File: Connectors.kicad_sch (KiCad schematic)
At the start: 4 parts

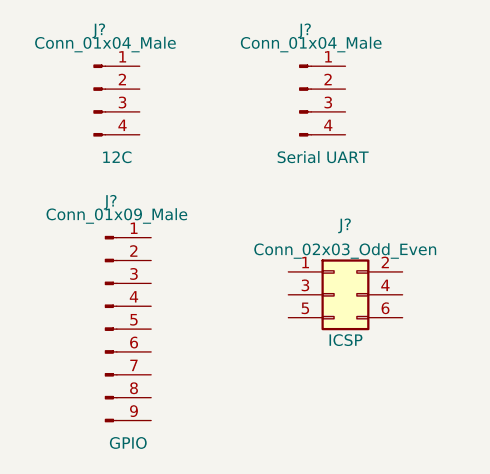
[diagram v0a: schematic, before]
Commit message: Changed locations of symbols
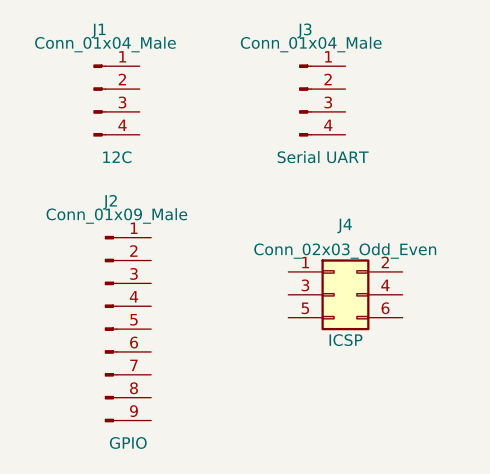
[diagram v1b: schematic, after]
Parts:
- gave numbers to parts that had none: 4
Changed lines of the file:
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@@
   (symbol (lib_id "Connector_Generic:Conn_02x03_Odd_Even") (at 111.76 92.71 0) (unit 1)
     (in_bom yes) (on_board yes)
-    (property "Reference" "J?" (id 0) (at 113.03 84.9335 0))
+    (property "Reference" "J4" (id 0) (at 113.03 84.9335 0))
     (property "Value" "Conn_02x03_Odd_Even" (id 1) (at 113.03 87.7086 0))
     (property "Footprint" "" (id 2) (at 111.76 92.71 0)
@@
   (symbol (lib_id "Connector:Conn_01x04_Male") (at 107.95 69.85 0) (unit 1)
     (in_bom yes) (on_board yes)
-    (property "Reference" "J?" (id 0) (at 108.585 63.2673 0))
+    (property "Reference" "J3" (id 0) (at 108.585 63.2673 0))
     (property "Value" "Conn_01x04_Male" (id 1) (at 109.22 64.77 0))
     (property "Footprint" "" (id 2) (at 107.95 69.85 0)
@@
   (symbol (lib_id "Connector:Conn_01x09_Male") (at 86.36 96.52 0) (unit 1)
     (in_bom yes) (on_board yes)
-    (property "Reference" "J?" (id 0) (at 86.995 82.3173 0))
+    (property "Reference" "J2" (id 0) (at 86.995 82.3173 0))
     (property "Value" "Conn_01x09_Male" (id 1) (at 87.63 83.82 0))
     (property "Footprint" "" (id 2) (at 86.36 96.52 0)
@@
   (symbol (lib_id "Connector:Conn_01x04_Male") (at 85.09 69.85 0) (unit 1)
     (in_bom yes) (on_board yes)
-    (property "Reference" "J?" (id 0) (at 85.725 63.2673 0))
+    (property "Reference" "J1" (id 0) (at 85.725 63.2673 0))
     (property "Value" "Conn_01x04_Male" (id 1) (at 86.36 64.77 0))
     (property "Footprint" "" (id 2) (at 85.09 69.85 0)

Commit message: Completed symbol-footprint associations
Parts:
- J1, J3: footprint (none) -> Connector_PinHeader_2.54mm:PinHeader_1x04_P2.54mm_Vertical
- J2: footprint (none) -> Connector_PinHeader_2.54mm:PinHeader_1x09_P2.54mm_Vertical
- J4: footprint (none) -> Connector_PinHeader_2.54mm:PinHeader_2x03_P2.54mm_Vertical
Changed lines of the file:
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@@
     (property "Reference" "J4" (id 0) (at 113.03 84.9335 0))
     (property "Value" "Conn_02x03_Odd_Even" (id 1) (at 113.03 87.7086 0))
-    (property "Footprint" "" (id 2) (at 111.76 92.71 0)
+    (property "Footprint" "Connector_PinHeader_2.54mm:PinHeader_2x03_P2.54mm_Vertical" (id 2) (at 111.76 92.71 0)
       (effects (font (size 1.27 1.27)) hide)
     )
@@
     (property "Reference" "J3" (id 0) (at 108.585 63.2673 0))
     (property "Value" "Conn_01x04_Male" (id 1) (at 109.22 64.77 0))
-    (property "Footprint" "" (id 2) (at 107.95 69.85 0)
+    (property "Footprint" "Connector_PinHeader_2.54mm:PinHeader_1x04_P2.54mm_Vertical" (id 2) (at 107.95 69.85 0)
       (effects (font (size 1.27 1.27)) hide)
     )
@@
     (property "Reference" "J2" (id 0) (at 86.995 82.3173 0))
     (property "Value" "Conn_01x09_Male" (id 1) (at 87.63 83.82 0))
-    (property "Footprint" "" (id 2) (at 86.36 96.52 0)
+    (property "Footprint" "Connector_PinHeader_2.54mm:PinHeader_1x09_P2.54mm_Vertical" (id 2) (at 86.36 96.52 0)
       (effects (font (size 1.27 1.27)) hide)
     )
@@
     (property "Reference" "J1" (id 0) (at 85.725 63.2673 0))
     (property "Value" "Conn_01x04_Male" (id 1) (at 86.36 64.77 0))
-    (property "Footprint" "" (id 2) (at 85.09 69.85 0)
+    (property "Footprint" "Connector_PinHeader_2.54mm:PinHeader_1x04_P2.54mm_Vertical" (id 2) (at 85.09 69.85 0)
       (effects (font (size 1.27 1.27)) hide)
     )

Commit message: final Wiring
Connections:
- net MISO: now reaches J4.1 (Pin_1)
- net Vcc: now reaches J4.2 (Pin_2)
- net Vcc: now also J1.2 (Pin_2), J2.9 (Pin_9), J3.2 (Pin_2)
- net SCK: now reaches J4.3 (Pin_3)
- net SCK: now also J1.4 (Pin_4)
- net MOSI: now reaches J4.4 (Pin_4)
- net RESET: now reaches J4.5 (Pin_5)
- net GND: now reaches J4.6 (Pin_6)
- net GND: now also J1.1 (Pin_1), J2.8 (Pin_8), J3.1 (Pin_1)
- net RX: now reaches J3.3 (Pin_3)
- net TX: now reaches J3.4 (Pin_4)
- net D2: now reaches J2.1 (Pin_1)
- net D3: now reaches J2.2 (Pin_2)
- net D4: now reaches J2.3 (Pin_3)
- net D5: now reaches J2.4 (Pin_4)
- net D6: now reaches J2.5 (Pin_5)
- net D7: now reaches J2.6 (Pin_6)
- net D8: now reaches J2.7 (Pin_7)
- net SDA: now reaches J1.3 (Pin_3)
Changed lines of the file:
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@@
 (kicad_sch (version 20211123) (generator eeschema)
   (paper "A4")
+  (hierarchical_label "RX" (shape input) (at 113.03 72.39 0)
+    (effects (font (size 1.27 1.27)) (justify left))
+  )
+  (hierarchical_label "SCK" (shape passive) (at 106.68 92.71 180)
+    (effects (font (size 1.27 1.27)) (justify right))
+  )
+  (hierarchical_label "GND" (shape passive) (at 91.44 104.14 0)
+    (effects (font (size 1.27 1.27)) (justify left))
+  )
+  (hierarchical_label "SDA" (shape bidirectional) (at 90.17 72.39 0)
+    (effects (font (size 1.27 1.27)) (justify left))
+  )
+  (hierarchical_label "Vcc" (shape passive) (at 119.38 90.17 0)
+    (effects (font (size 1.27 1.27)) (justify left))
+  )
+  (hierarchical_label "D7" (shape bidirectional) (at 91.44 99.06 0)
+    (effects (font (size 1.27 1.27)) (justify left))
+  )
+  (hierarchical_label "SCK" (shape passive) (at 90.17 74.93 0)
+    (effects (font (size 1.27 1.27)) (justify left))
+  )
+  (hierarchical_label "GND" (shape passive) (at 113.03 67.31 0)
+    (effects (font (size 1.27 1.27)) (justify left))
+  )
+  (hierarchical_label "Vcc" (shape passive) (at 91.44 106.68 0)
+    (effects (font (size 1.27 1.27)) (justify left))
+  )
+  (hierarchical_label "D5" (shape bidirectional) (at 91.44 93.98 0)
+    (effects (font (size 1.27 1.27)) (justify left))
+  )
+  (hierarchical_label "GND" (shape passive) (at 90.17 67.31 0)
+    (effects (font (size 1.27 1.27)) (justify left))
+  )
+  (hierarchical_label "TX" (shape output) (at 113.03 74.93 0)
+    (effects (font (size 1.27 1.27)) (justify left))
+  )
+  (hierarchical_label "MOSI" (shape input) (at 119.38 92.71 0)
+    (effects (font (size 1.27 1.27)) (justify left))
+  )
+  (hierarchical_label "MISO" (shape output) (at 106.68 90.17 180)
+    (effects (font (size 1.27 1.27)) (justify right))
+  )
+  (hierarchical_label "Vcc" (shape passive) (at 90.17 69.85 0)
+    (effects (font (size 1.27 1.27)) (justify left))
+  )
+  (hierarchical_label "RESET" (shape passive) (at 106.68 95.25 180)
+    (effects (font (size 1.27 1.27)) (justify right))
+  )
+  (hierarchical_label "D2" (shape bidirectional) (at 91.44 86.36 0)
+    (effects (font (size 1.27 1.27)) (justify left))
+  )
+  (hierarchical_label "D8" (shape bidirectional) (at 91.44 101.6 0)
+    (effects (font (size 1.27 1.27)) (justify left))
+  )
+  (hierarchical_label "D4" (shape bidirectional) (at 91.44 91.44 0)
+    (effects (font (size 1.27 1.27)) (justify left))
+  )
+  (hierarchical_label "Vcc" (shape passive) (at 113.03 69.85 0)
+    (effects (font (size 1.27 1.27)) (justify left))
+  )
+  (hierarchical_label "GND" (shape passive) (at 119.38 95.25 0)
+    (effects (font (size 1.27 1.27)) (justify left))
+  )
+  (hierarchical_label "D3" (shape bidirectional) (at 91.44 88.9 0)
+    (effects (font (size 1.27 1.27)) (justify left))
+  )
+  (hierarchical_label "D6" (shape bidirectional) (at 91.44 96.52 0)
+    (effects (font (size 1.27 1.27)) (justify left))
+  )
   (symbol (lib_id "Connector_Generic:Conn_02x03_Odd_Even") (at 111.76 92.71 0) (unit 1)
     (in_bom yes) (on_board yes)
